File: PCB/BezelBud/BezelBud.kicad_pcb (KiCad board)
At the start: 4 copper layers, 70.1 x 39.6 mm, 71 parts, among them J1 USB_C_Receptacle_USB2.0_16P, J2 Conn_01x05_Pin, SW1 SW_SPDT, SW2 SW_SPDT, SW3 SW_SPDT, SW4 SW_SPDT, SW5 SW_SPDT, SW6 SW_SPDT, SW7 SW_SPDT, SW8 SW_SPDT, SW9 SW_SPDT, U1 STM32G431CBT6, U2 USBLC6-2SC6, U3 LP5907MFX-3.3, U4 LP5907MFX-3.3, U5 PCM1861DBT, Y1 Crystal_GND24

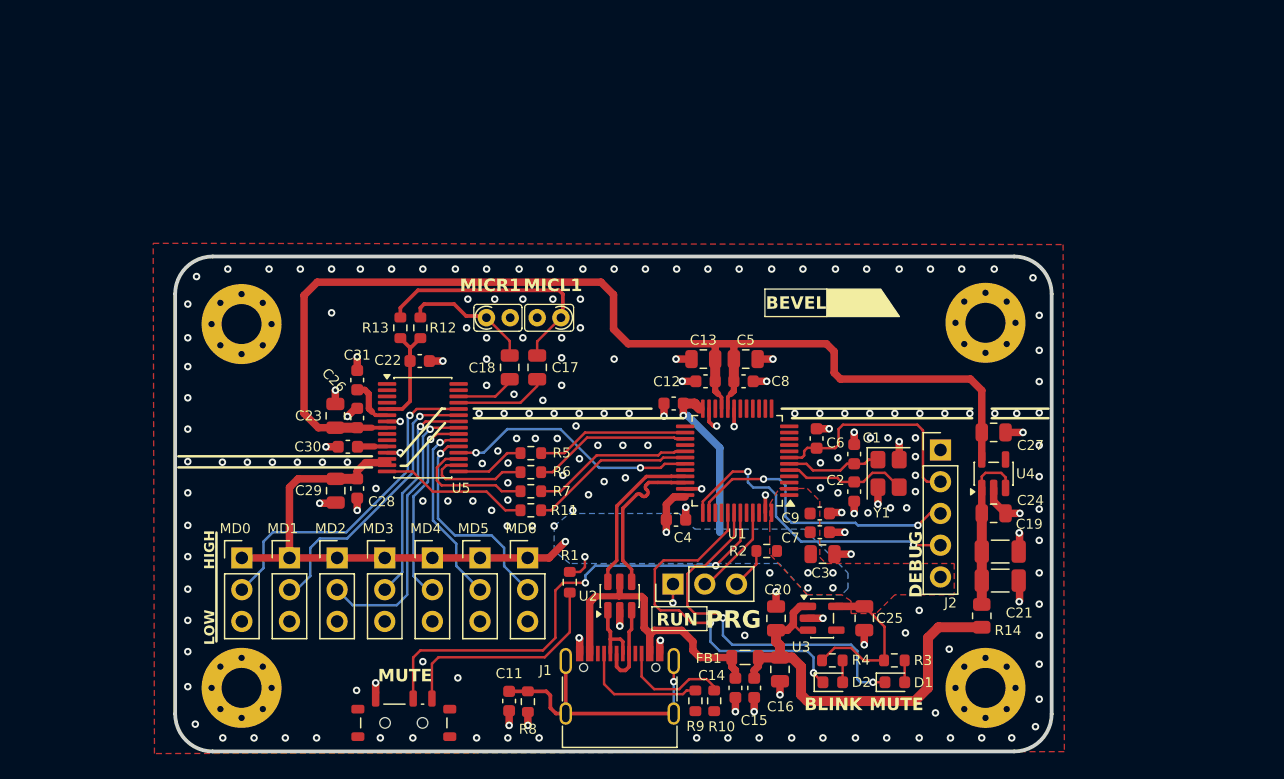
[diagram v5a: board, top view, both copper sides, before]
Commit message: remapped int pin to avoid crossing
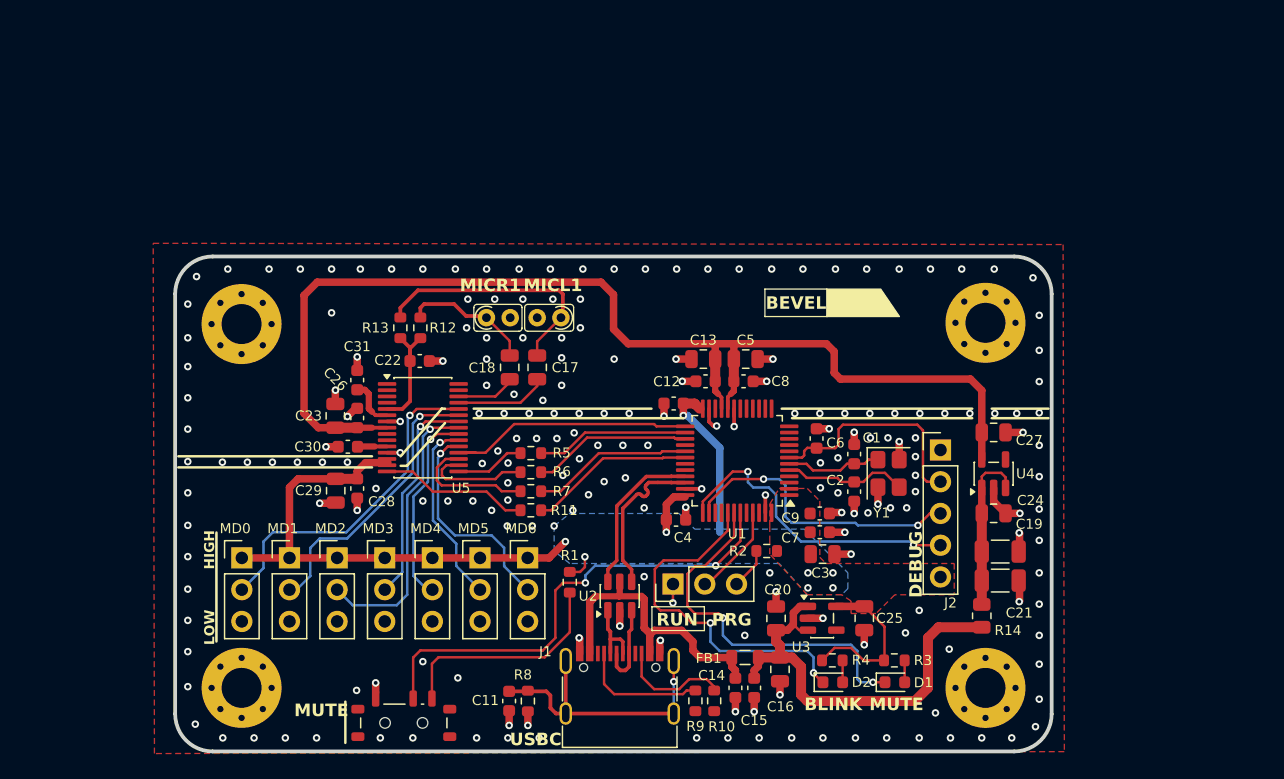
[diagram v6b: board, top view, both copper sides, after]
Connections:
- U1 pad 25: unconnected-(U1-PB11-Pad25) -> INT
- U1 pad 31: INT -> unconnected-(U1-PA9-Pad31)
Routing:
- net INT: track 20.3 -> 20.5 mm, vias 2 -> 0
- net GND: vias 208 -> 210
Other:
- board text added: "USBC"

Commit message: removed usb decoupling and moved blink and led vias
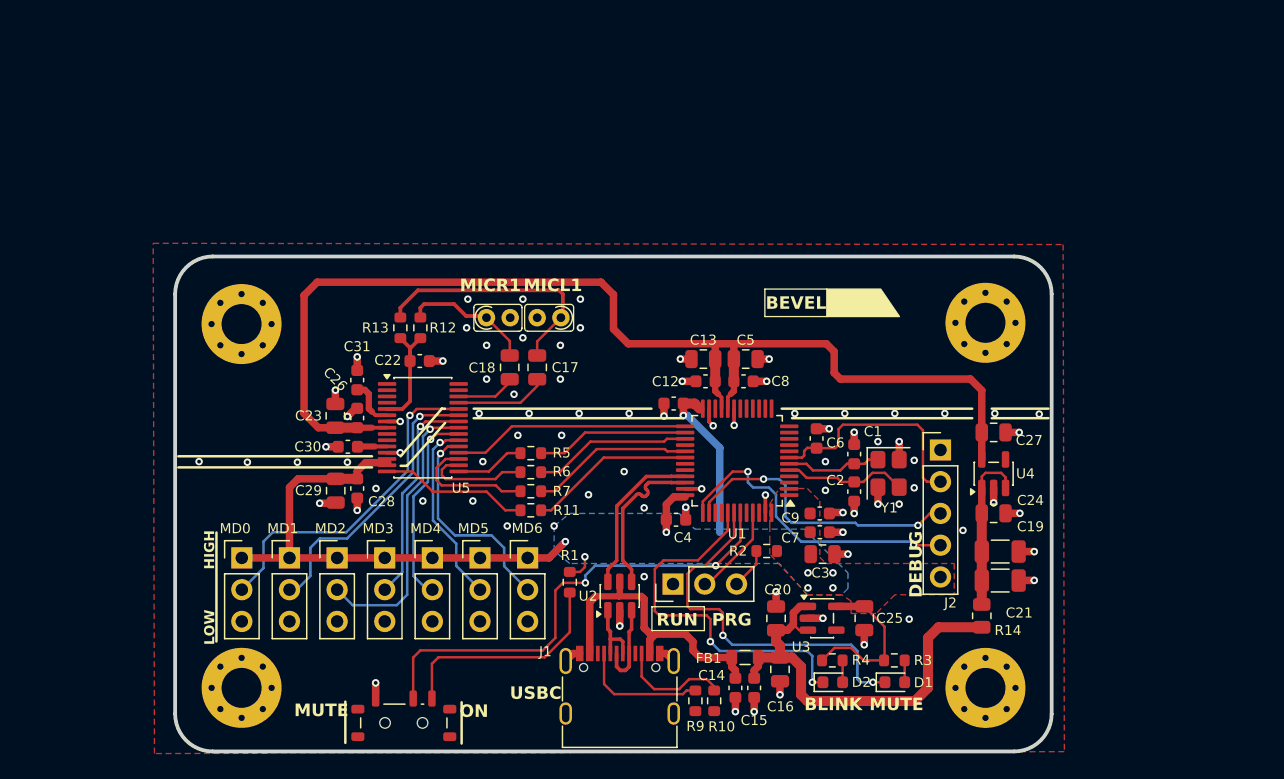
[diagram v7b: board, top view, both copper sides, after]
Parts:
- removed C11: 0.1uF, Capacitor_SMD:C_0603_1608Metric
- removed R8: 1M, Resistor_SMD:R_0603_1608Metric
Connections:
- J1 pad S1: /SHIELD -> GND
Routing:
- net /SHIELD: track 22.9 -> 0.00 mm, vias 1 -> 0
- net GND: track 54.7 -> 47.6 mm, vias 210 -> 85
- net INT: track 20.5 -> 19.0 mm
- net /LED_BLINK: track 29.0 -> 30.0 mm
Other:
- board text added: "ON"
- board text added: "Reviewed By: SimonPatterson Whitebowfr Strong-Mud199"

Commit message: updated size of pcb to be round numbers
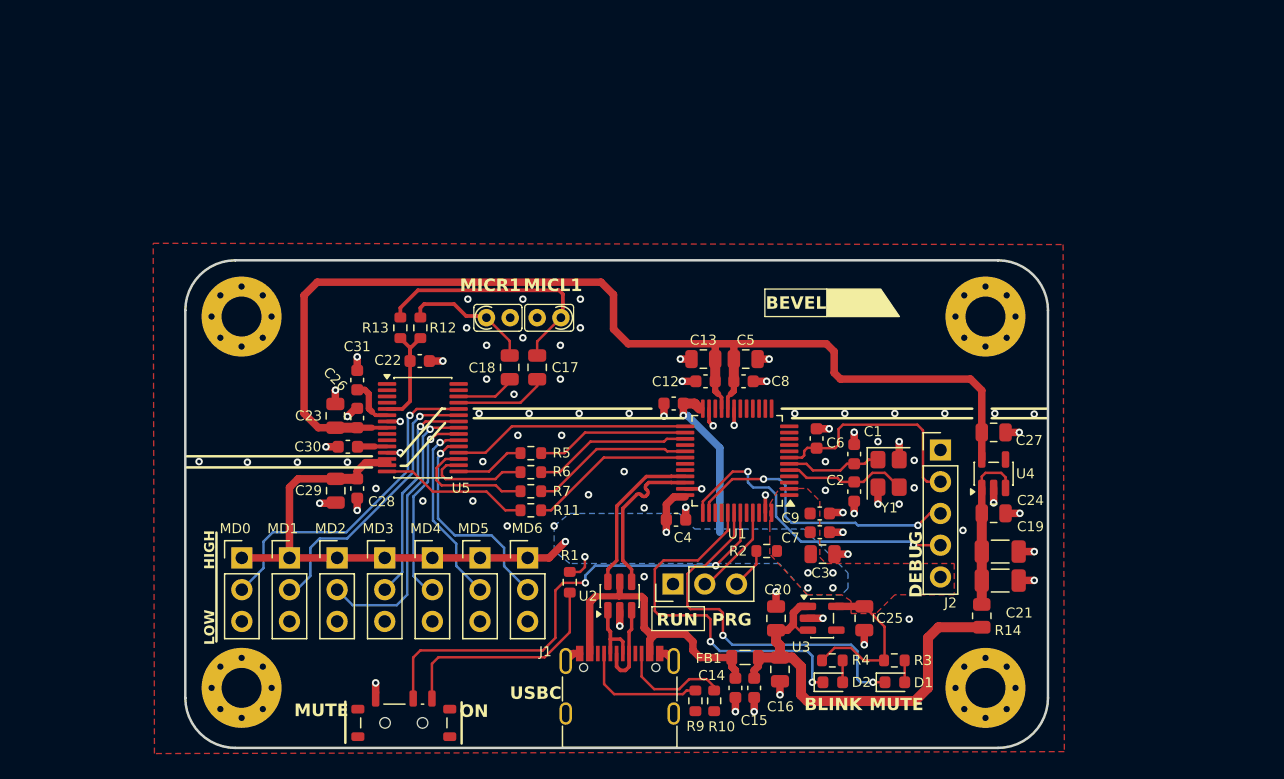
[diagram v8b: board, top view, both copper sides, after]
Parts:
- moved H1 0.60 mm to (112.5, 63.5)
- moved H2 0.50 mm to (172.0, 63.5)
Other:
- board size 70.1 x 39.6 mm -> 69 x 39 mm
